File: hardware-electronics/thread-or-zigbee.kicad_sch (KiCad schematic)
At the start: 28 parts, among them J3 CONMHF1-SMD-T, U5 CP2102N-A02-GQFN20, U7 EFR32MG21B020F1024IM32-B, Y4 ABM8-38.400MHZ-10-D1G-T

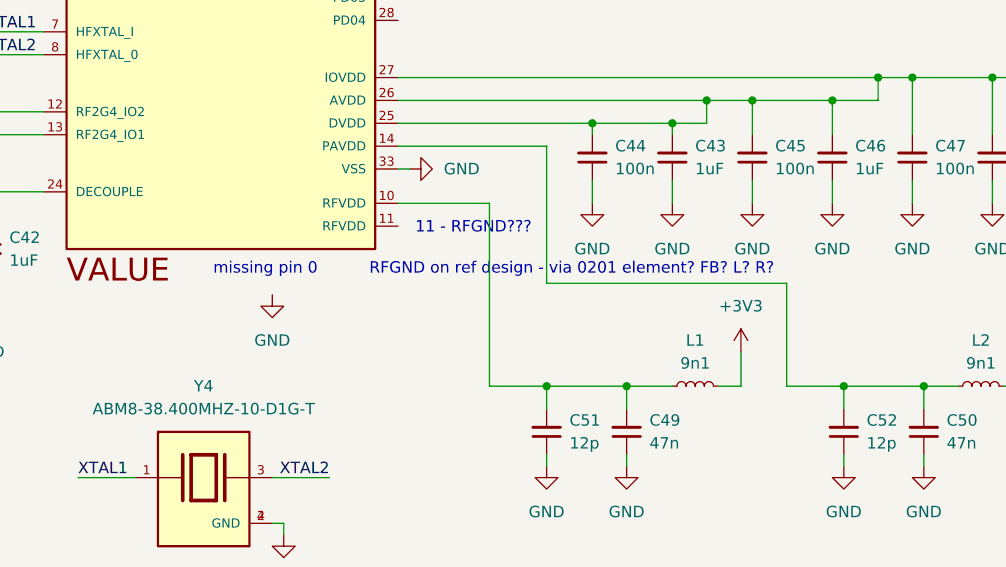
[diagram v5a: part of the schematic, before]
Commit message: [#12] SCH thread/zigbee EFR32 fixed wrong pin name
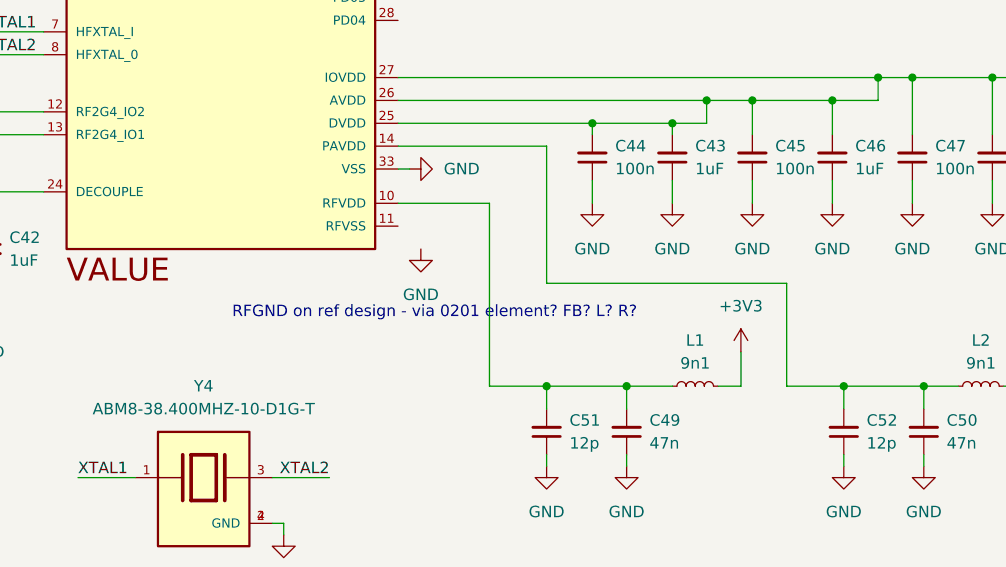
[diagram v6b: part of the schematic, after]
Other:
- note removed: "11 - RFGND???"
- note removed: "missing pin 0"
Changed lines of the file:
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@@
 		)
 	)
-	(text "missing pin 0"
-		(exclude_from_sim no)
-		(at 187.198 114.046 0)
-		(effects
-			(font
-				(size 1.27 1.27)
-			)
-		)
-	)
 	(text "why C on NC on ref design?\nEMI reduction?"
 		(exclude_from_sim no)
@@
 		)
 	)
-	(text "11 - RFGND???"
-		(exclude_from_sim no)
-		(at 210.312 109.474 0)
-		(effects
-			(font
-				(size 1.27 1.27)
-			)
-		)
-	)
 	(text "RFGND on ref design - via 0201 element? FB? L? R?"
 		(exclude_from_sim no)
-		(at 221.234 114.046 0)
+		(at 205.994 118.872 0)
 		(effects
 			(font
@@
 	(symbol
 		(lib_id "power:GND")
-		(at 187.96 116.84 0)
+		(at 204.47 111.76 0)
 		(unit 1)
 		(exclude_from_sim no)
@@
 		(fields_autoplaced yes)
 		(property "Reference" "#PWR0102"
-			(at 187.96 123.19 0)
+			(at 204.47 118.11 0)
 			(effects
 				(font
@@
 		)
 		(property "Value" "GND"
-			(at 187.96 121.92 0)
+			(at 204.47 116.84 0)
 			(effects
 				(font
@@
 		)
 		(property "Footprint" ""
-			(at 187.96 116.84 0)
+			(at 204.47 111.76 0)
 			(effects
 				(font
@@
 		)
 		(property "Datasheet" ""
-			(at 187.96 116.84 0)
+			(at 204.47 111.76 0)
 			(effects
 				(font
@@
 		)
 		(property "Description" "Power symbol creates a global label with name \"GND\" , ground"
-			(at 187.96 116.84 0)
+			(at 204.47 111.76 0)
 			(effects
 				(font

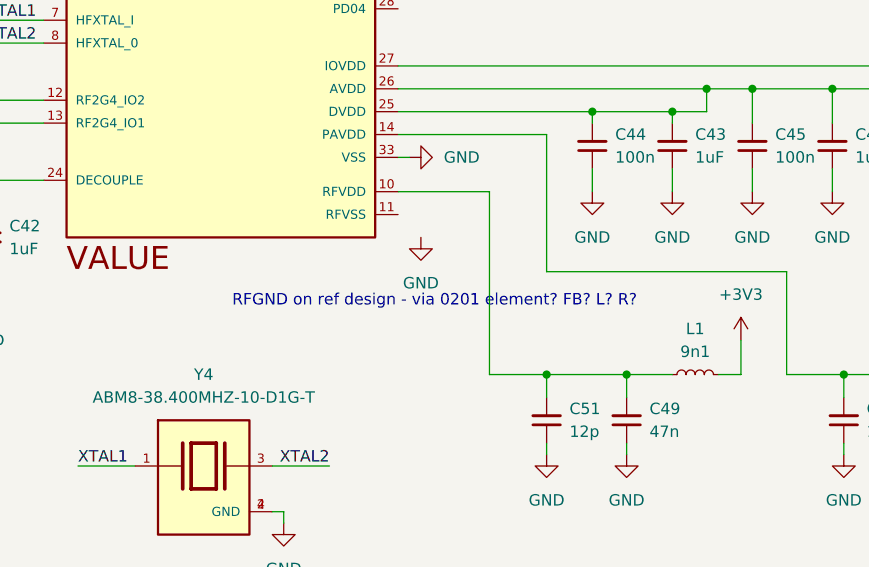
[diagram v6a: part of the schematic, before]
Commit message: [#12] SCH thread/zigbee EFR32 add FB on RF GND
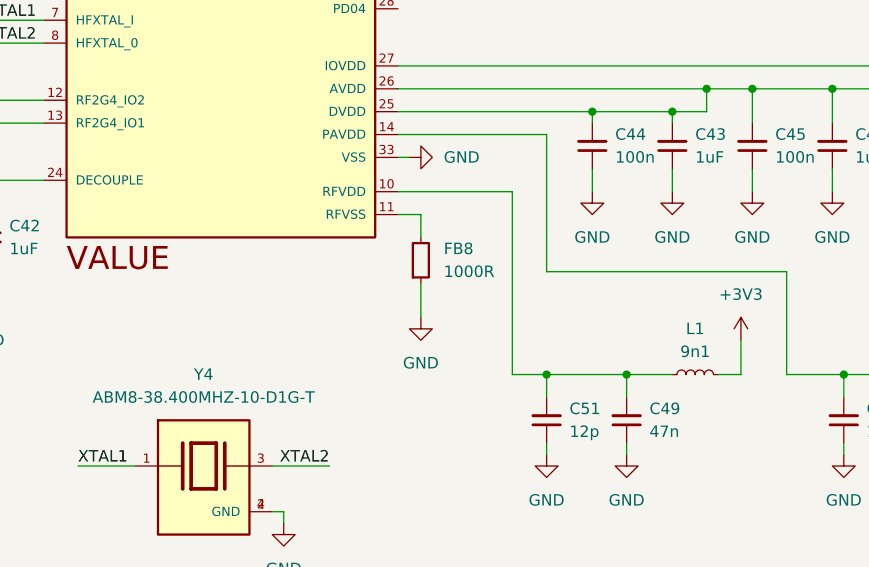
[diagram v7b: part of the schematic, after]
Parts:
- added FB8: FB_1000R_0402, FB_1000R_0402:FB_0402_1005Metric, symbol M2SmartHomeSymbols:FB_1000R_0402
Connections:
- net GND: now also FB8.1
- net at U7.11 (RFVSS): now also FB8.2
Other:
- note removed: "RFGND on ref design - via 0201 element? FB? L? R?"
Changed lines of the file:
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@@
 	(wire
 		(pts
+			(xy 204.47 109.22) (xy 204.47 111.76)
+		)
+		(stroke
+			(width 0)
+			(type default)
+		)
+	)
+	(wire
+		(pts
+			(xy 201.93 109.22) (xy 204.47 109.22)
+		)
+		(stroke
+			(width 0)
+			(type default)
+		)
+	)
+	(wire
+		(pts
 			(xy 27.94 48.26) (xy 27.94 49.53)
 		)
@@
 	(wire
 		(pts
-			(xy 212.09 127) (xy 218.44 127)
+			(xy 214.63 127) (xy 218.44 127)
 		)
 		(stroke
@@
 	(wire
 		(pts
+			(xy 204.47 116.84) (xy 204.47 120.65)
+		)
+		(stroke
+			(width 0)
+			(type default)
+		)
+	)
+	(wire
+		(pts
 			(xy 52.07 68.58) (xy 43.18 68.58)
 		)
@@
 	(wire
 		(pts
-			(xy 212.09 106.68) (xy 212.09 127)
+			(xy 214.63 106.68) (xy 214.63 127)
 		)
 		(stroke
@@
 	(wire
 		(pts
-			(xy 201.93 106.68) (xy 212.09 106.68)
+			(xy 201.93 106.68) (xy 214.63 106.68)
 		)
 		(stroke
@@
 		)
 	)
-	(text "RFGND on ref design - via 0201 element? FB? L? R?"
-		(exclude_from_sim no)
-		(at 205.994 118.872 0)
-		(effects
-			(font
-				(size 1.27 1.27)
-			)
-		)
-	)
 	(text "verify matching network with PCB stack-up"
 		(exclude_from_sim no)
@@
 	(symbol
 		(lib_id "power:GND")
-		(at 204.47 111.76 0)
+		(at 204.47 120.65 0)
 		(unit 1)
 		(exclude_from_sim no)
@@
 		(fields_autoplaced yes)
 		(property "Reference" "#PWR0102"
-			(at 204.47 118.11 0)
+			(at 204.47 127 0)
 			(effects
 				(font
@@
 		)
 		(property "Value" "GND"
-			(at 204.47 116.84 0)
+			(at 204.47 125.73 0)
 			(effects
 				(font
@@
 		)
 		(property "Footprint" ""
-			(at 204.47 111.76 0)
+			(at 204.47 120.65 0)
 			(effects
 				(font
@@
 		)
 		(property "Datasheet" ""
-			(at 204.47 111.76 0)
+			(at 204.47 120.65 0)
 			(effects
 				(font
@@
 		)
 		(property "Description" "Power symbol creates a global label with name \"GND\" , ground"
-			(at 204.47 111.76 0)
+			(at 204.47 120.65 0)
 			(effects
 				(font
@@
 					(unit 1)
 				)
+			)
+		)
+	)
+	(symbol
+		(lib_id "M2SmartHomeSymbols:FB_1000R_0402")
+		(at 204.47 116.84 90)
+		(unit 1)
+		(exclude_from_sim no)
+		(in_bom yes)
+		(on_board yes)
+		(dnp no)
+		(fields_autoplaced yes)
+		(property "Reference" "FB8"
+			(at 207.01 113.03 90)
+			(effects
+				(font
+					(size 1.27 1.27)
+					(thickness 0.15)
+				)
+				(justify right)
+			)
+		)
+		(property "Value" "FB_1000R_0402"
+			(at 214.63 96.52 0)
+			(effects
+				(font
+					(size 1.27 1.27)
+					(thickness 0.15)
+				)
+				(justify left bottom)
+				(hide yes)
+			)
+		)
+		(property "Footprint" "FB_1000R_0402:FB_0402_1005Metric"
+			(at 217.17 96.52 0)
+			(effects
+				(font
+					(size 1.27 1.27)
+					(thickness 0.15)
+				)
+				(justify left bottom)
+				(hide yes)
+			)
+		)
+		(property "Datasheet" "https://www.murata.com/products/productdetail?partno=BLM15HG102SN1D"
+			(at 219.71 96.52 0)
+			(effects
+				(font
+					(size 1.27 1.27)
+					(thickness 0.15)
+				)
+				(justify left bottom)
+				(hide yes)
+			)
+		)
+		(property "Description" "SMD Ferrite Bead, 1000 Ω at 100 MHz, 200 mA, 0.6 Ω max, 0402 [1005 Metric], BLM15H Series"
+			(at 204.47 116.84 0)
+			(effects
+				(font
+					(size 1.27 1.27)
+				)
+				(hide yes)
+			)
+		)
+		(property "MPN" "BLM15HG102SN1D"
+			(at 222.25 96.52 0)
+			(effects
+				(font
+					(size 1.27 1.27)
+					(thickness 0.15)
+				)
+				(justify left bottom)
+				(hide yes)
+			)
+		)
+		(property "Manufacturer" "Murata"
+			(at 224.79 96.52 0)
+			(effects
+				(font
+					(size 1.27 1.27)
+					(thickness 0.15)
+				)
+				(justify left bottom)
+				(hide yes)
+			)
+		)
+		(property "License" "Apache-2.0"
+			(at 227.33 96.52 0)
+			(effects
+				(font
+					(size 1.27 1.27)
+					(thickness 0.15)
+				)
+				(justify left bottom)
+				(hide yes)
+			)
+		)
+		(property "Author" "Your Name"
+			(at 229.87 96.52 0)
+			(effects
+				(font
+					(size 1.27 1.27)
+					(thickness 0.15)
+				)
+				(justify left bottom)
+				(hide yes)
+			)
+		)
+		(property "Val" "1000R"
+			(at 207.01 115.57 90)
+			(effects
+				(font
+					(size 1.27 1.27)
+					(thickness 0.15)
+				)
+				(justify right)
+			)
+		)
+		(property "Impedance" "1000 Ω @ 100 MHz"
+			(at 214.63 96.52 0)
+			(effects
+				(font
+					(size 1.27 1.27)
+				)
+				(justify left bottom)
+				(hide yes)
+			)
+		)
+		(property "Current" "200 mA"
+			(at 218.17 96.52 0)
+			(effects
+				(font
+					(size 1.27 1.27)
+				)
+				(justify left bottom)
+				(hide yes)
+			)
+		)
+		(pin "1"
+		)
+		(pin "2"
+		)
+		(instances
+			(project "M2SmartHome"
+				(path "/da663dec-9e91-4003-a791-431d460ad63c/a351a459-aa5d-43cb-82d3-d5bdf9396bea"
+					(reference "FB8")
+					(unit 1)
+				)

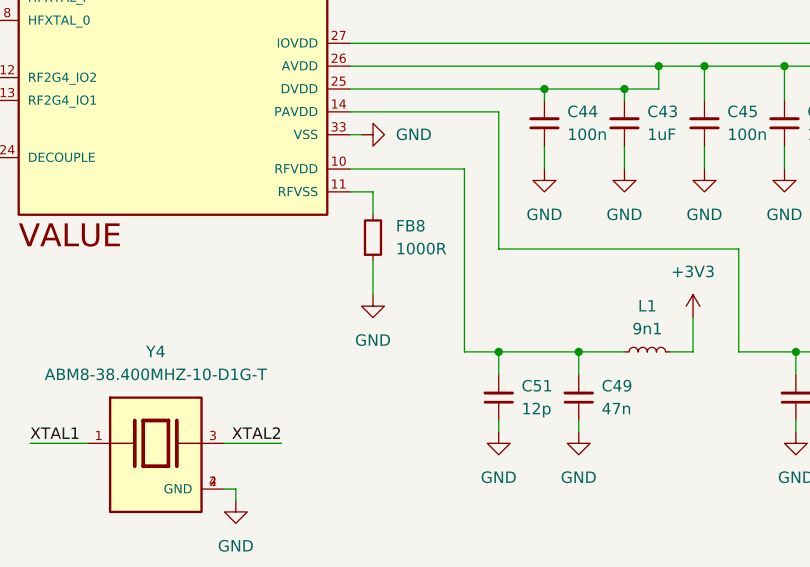
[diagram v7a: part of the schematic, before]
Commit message: [#9] SCH wifi add RTL8188FTV-VC-CG
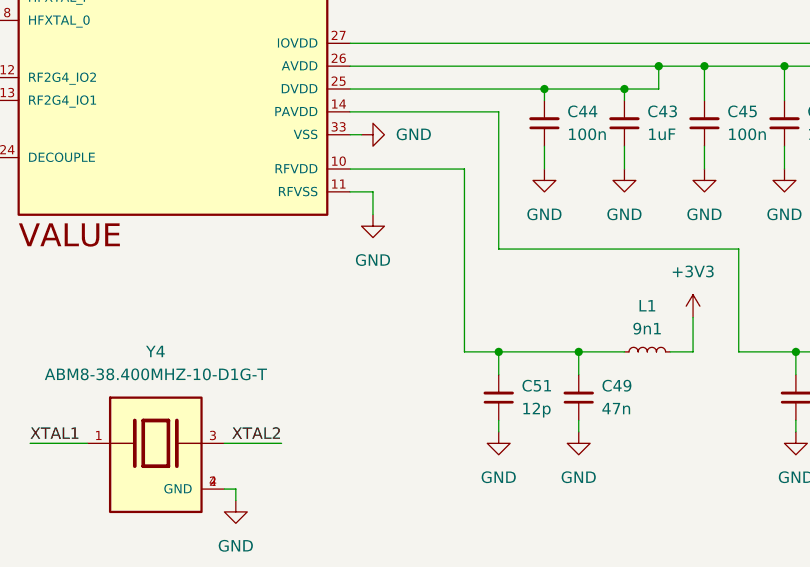
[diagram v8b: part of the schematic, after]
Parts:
- removed FB8: FB_1000R_0402, FB_1000R_0402:FB_0402_1005Metric, symbol M2SmartHomeSymbols:FB_1000R_0402
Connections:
- net GND: now also U7.11 (RFVSS)
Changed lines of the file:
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@@
 	(wire
 		(pts
-			(xy 204.47 116.84) (xy 204.47 120.65)
-		)
-		(stroke
-			(width 0)
-			(type default)
-		)
-	)
-	(wire
-		(pts
 			(xy 52.07 68.58) (xy 43.18 68.58)
 		)
@@
 	(symbol
 		(lib_id "power:GND")
-		(at 204.47 120.65 0)
+		(at 204.47 111.76 0)
 		(unit 1)
 		(exclude_from_sim no)
@@
 		(fields_autoplaced yes)
 		(property "Reference" "#PWR0102"
-			(at 204.47 127 0)
+			(at 204.47 118.11 0)
 			(effects
 				(font
@@
 		)
 		(property "Value" "GND"
-			(at 204.47 125.73 0)
+			(at 204.47 116.84 0)
 			(effects
 				(font
@@
 		)
 		(property "Footprint" ""
-			(at 204.47 120.65 0)
+			(at 204.47 111.76 0)
 			(effects
 				(font
@@
 		)
 		(property "Datasheet" ""
-			(at 204.47 120.65 0)
+			(at 204.47 111.76 0)
 			(effects
 				(font
@@
 		)
 		(property "Description" "Power symbol creates a global label with name \"GND\" , ground"
-			(at 204.47 120.65 0)
+			(at 204.47 111.76 0)
 			(effects
 				(font
@@
 					(unit 1)
 				)
-			)
-		)
-	)
-	(symbol
-		(lib_id "M2SmartHomeSymbols:FB_1000R_0402")
-		(at 204.47 116.84 90)
-		(unit 1)
-		(exclude_from_sim no)
-		(in_bom yes)
-		(on_board yes)
-		(dnp no)
-		(fields_autoplaced yes)
-		(property "Reference" "FB8"
-			(at 207.01 113.03 90)
-			(effects
-				(font
-					(size 1.27 1.27)
-					(thickness 0.15)
-				)
-				(justify right)
-			)
-		)
-		(property "Value" "FB_1000R_0402"
-			(at 214.63 96.52 0)
-			(effects
-				(font
-					(size 1.27 1.27)
-					(thickness 0.15)
-				)
-				(justify left bottom)
-				(hide yes)
-			)
-		)
-		(property "Footprint" "FB_1000R_0402:FB_0402_1005Metric"
-			(at 217.17 96.52 0)
-			(effects
-				(font
-					(size 1.27 1.27)
-					(thickness 0.15)
-				)
-				(justify left bottom)
-				(hide yes)
-			)
-		)
-		(property "Datasheet" "https://www.murata.com/products/productdetail?partno=BLM15HG102SN1D"
-			(at 219.71 96.52 0)
-			(effects
-				(font
-					(size 1.27 1.27)
-					(thickness 0.15)
-				)
-				(justify left bottom)
-				(hide yes)
-			)
-		)
-		(property "Description" "SMD Ferrite Bead, 1000 Ω at 100 MHz, 200 mA, 0.6 Ω max, 0402 [1005 Metric], BLM15H Series"
-			(at 204.47 116.84 0)
-			(effects
-				(font
-					(size 1.27 1.27)
-				)
-				(hide yes)
-			)
-		)
-		(property "MPN" "BLM15HG102SN1D"
-			(at 222.25 96.52 0)
-			(effects
-				(font
-					(size 1.27 1.27)
-					(thickness 0.15)
-				)
-				(justify left bottom)
-				(hide yes)
-			)
-		)
-		(property "Manufacturer" "Murata"
-			(at 224.79 96.52 0)
-			(effects
-				(font
-					(size 1.27 1.27)
-					(thickness 0.15)
-				)
-				(justify left bottom)
-				(hide yes)
-			)
-		)
-		(property "License" "Apache-2.0"
-			(at 227.33 96.52 0)
-			(effects
-				(font
-					(size 1.27 1.27)
-					(thickness 0.15)
-				)
-				(justify left bottom)
-				(hide yes)
-			)
-		)
-		(property "Author" "Your Name"
-			(at 229.87 96.52 0)
-			(effects
-				(font
-					(size 1.27 1.27)
-					(thickness 0.15)
-				)
-				(justify left bottom)
-				(hide yes)
-			)
-		)
-		(property "Val" "1000R"
-			(at 207.01 115.57 90)
-			(effects
-				(font
-					(size 1.27 1.27)
-					(thickness 0.15)
-				)
-				(justify right)
-			)
-		)
-		(property "Impedance" "1000 Ω @ 100 MHz"
-			(at 214.63 96.52 0)
-			(effects
-				(font
-					(size 1.27 1.27)
-				)
-				(justify left bottom)
-				(hide yes)
-			)
-		)
-		(property "Current" "200 mA"
-			(at 218.17 96.52 0)
-			(effects
-				(font
-					(size 1.27 1.27)
-				)
-				(justify left bottom)
-				(hide yes)
-			)
-		)
-		(pin "1"
-		)
-		(pin "2"
-		)
-		(instances
-			(project "M2SmartHome"
-				(path "/da663dec-9e91-4003-a791-431d460ad63c/a351a459-aa5d-43cb-82d3-d5bdf9396bea"
-					(reference "FB8")
-					(unit 1)
-				)
